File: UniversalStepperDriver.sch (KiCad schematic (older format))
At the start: 80 parts, among them P1 USB_OTG, P11 CONN_01X04, P12 CONN_01X02, P13 CONN_28BYJ-48, P14 CONN_28BYJ-48, P15 CONN_28BYJ-48, P17 CONN_01X04, P2 CONN_01X02, P3 CONN_01X02, P4 CONN_01X03, P5 Universal_Serial_Connector, P6 CONN_01X06, P7 RPI_header, P8 CONN_01X03, P9 CONN_01X04, SW1 SW_PUSH, SW2 SW_PUSH, SW3 SW_PUSH, U1 STM32F411RE, U2 INA169, U3 MPQ4420, U4 ULN2003V, U5 ULN2003V, Y1 CRYSTAL_SMD

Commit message: all connected
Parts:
- SW1: footprint Buttons_Switches_SMD:SW_SPST_SKQG -> KSEK43J_LFS_TACTILE_SWITCH:KSEK43J_LFS_TACTILE_SWITCH
- SW2, SW3: footprint Buttons_Switches_SMD:SW_SPST_EVQP7C -> Buttons_Switches_ThroughHole:SW_Tactile_SPST_Angled
- Y1: value CRYSTAL_SMD -> CRYSTAL_SMD_16MHz
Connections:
- net labels removed: X_MAX, Y_MAX
- wire segments 273 -> 272
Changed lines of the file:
@@
 F 0 "SW2" H 9500 10110 50  0000 C CNN
 F 1 "SW_PUSH" H 9350 9920 50  0000 C CNN
-F 2 "Buttons_Switches_SMD:SW_SPST_EVQP7C" H 9350 10000 50  0001 C CNN
+F 2 "Buttons_Switches_ThroughHole:SW_Tactile_SPST_Angled" H 9350 10000 50  0001 C CNN
 F 3 "www.ck-components.com/80185/pts840_5aug13.pdf/" H 9350 10000 50  0001 C CNN
 	1    9350 10000
@@
 F 0 "SW3" H 10925 10110 50  0000 C CNN
 F 1 "SW_PUSH" H 10775 9920 50  0000 C CNN
-F 2 "Buttons_Switches_SMD:SW_SPST_EVQP7C" H 10775 10000 50  0001 C CNN
+F 2 "Buttons_Switches_ThroughHole:SW_Tactile_SPST_Angled" H 10775 10000 50  0001 C CNN
 F 3 "www.ck-components.com/80185/pts840_5aug13.pdf/" H 10775 10000 50  0001 C CNN
 	1    10775 10000
@@
 P 8200 7400
 F 0 "Y1" V 8200 7490 50  0000 C CNN
-F 1 "CRYSTAL_SMD" V 8225 6700 50  0000 L CNN
+F 1 "CRYSTAL_SMD_16MHz" V 8200 6475 50  0000 L CNN
 F 2 ".pretty:SPK5032" H 8200 7400 50  0001 C CNN
 F 3 "https://www.sparkfun.com/datasheets/Components/SPK-5032-16MHZ.pdf" H 8200 7400 50  0001 C CNN
@@
 $EndComp
 Text Label 8750 10000 0    60   ~ 0
-X_MAX
+X_LIMIT
 Text Label 10150 10000 0    60   ~ 0
-Y_MAX
+Y_LIMIT
 $Comp
 L GND #PWR068
@@
 F 0 "SW1" H 10850 4210 50  0000 C CNN
 F 1 "SW_PUSH" H 10700 4020 50  0000 C CNN
-F 2 "Buttons_Switches_SMD:SW_SPST_SKQG" H 10700 4100 50  0001 C CNN
+F 2 "KSEK43J_LFS_TACTILE_SWITCH:KSEK43J_LFS_TACTILE_SWITCH" H 10700 4100 50  0001 C CNN
 F 3 "" H 10700 4100 50  0000 C CNN
 	1    10700 4100
@@
 EB 40 AE 91 C5 06 E4 9A 3A 2E B7 0D D5 1C 72 9D 41 C6 90 0B 35 38 47 11 CC 19 CA C2 9C 70 92 6E
 96 B2 30 A7 9C A4 5B 2F 80 A7 A3 53 25 FE 3F 24 8A F8 DE 8F 71 44 BF 00 00 00 00 49 45 4E 44 AE
-42 60 82 00
+42 60 82 0D
 EndData
 $EndBitmap
@@
 	4050 3850 4050 2925
 Wire Wire Line
-	3850 7500 3850 6650
+	3850 7375 3850 6650
 Wire Wire Line
 	3950 7600 3950 6650
@@
 	3225 7600 3950 7600
 Wire Wire Line
-	3225 7500 3850 7500
-Wire Wire Line
 	3750 6650 3750 7375

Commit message: rev0.1 board done
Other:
- note removed: "Mounting holes\n"
- moved on the sheet: C12, JP1, JP2, JP3, JP4, JP5, JP6, P5, R13, R15, SW2

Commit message: PWR LED add Fixes #3
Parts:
- added D3: LED_GREEN, LEDs:LED_0603, symbol LED
- added R6: 1k, Resistors_SMD:R_0603, symbol R
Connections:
- wire segments 272 -> 275

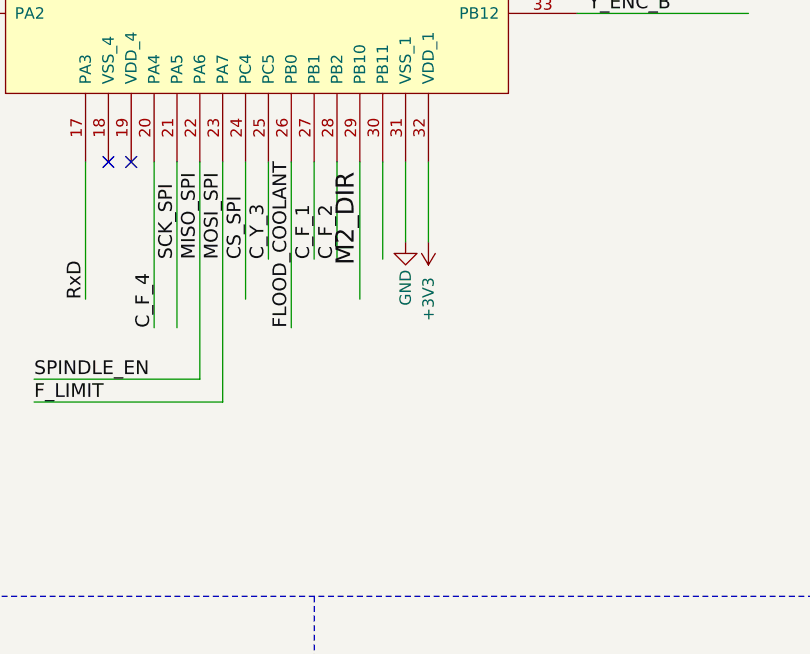
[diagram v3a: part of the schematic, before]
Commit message: add VCAP1 4.7u to PIN30(PB11) Fixes #2
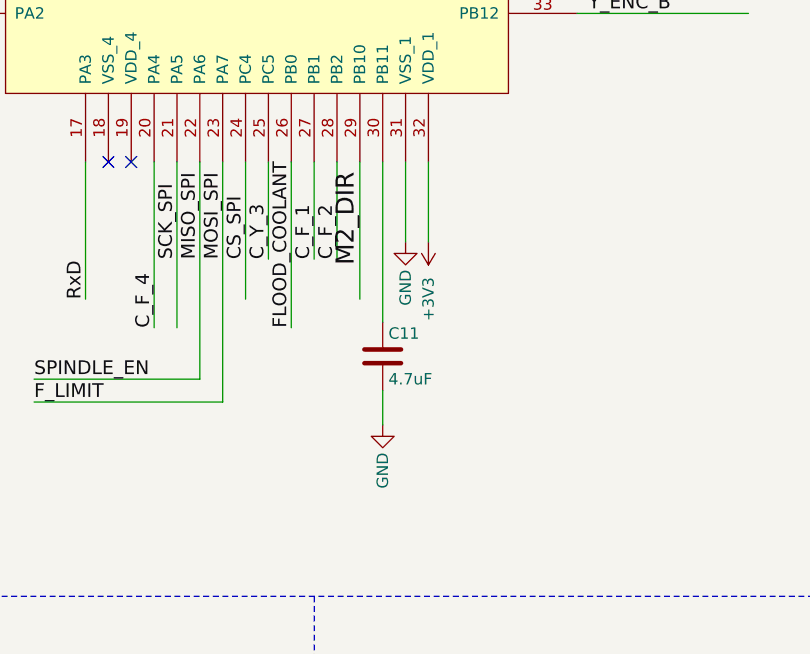
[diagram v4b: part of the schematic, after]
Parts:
- added C11: 4.7uF, Capacitors_SMD:C_0805, symbol C
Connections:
- wire segments 275 -> 276
